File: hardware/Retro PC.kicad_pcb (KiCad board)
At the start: 2 copper layers, 160 x 160 mm, 70 parts, among them IC1 74HC00, IC10 W65C22, IC2 W65C02, IC3 74HC138, IC4 SYSTEM ROM, IC5 RAM, IC6 W65C22, IC7 W65C51, IC8 TL7702, IC9 FT232RL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

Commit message: Add BOM and Schematics
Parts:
- moved C14 70.8 mm to (283.8, 165.3)
- moved C18 70.8 mm to (262.6, 199.3)
- moved C2 70.8 mm to (225.8, 105.5)
- moved D12 70.8 mm to (292.8, 159.9)
- moved D3 70.8 mm to (271.7, 63.7)
- moved D9 70.8 mm to (274.3, 128.8)
- moved IC10 70.8 mm to (211.1, 199.3)
- moved IC2 70.8 mm to (243.6, 109.8)
- moved R7 70.8 mm to (289.0, 159.9)
- moved SW3 70.8 mm to (219.2, 63.3)
- moved X4 70.8 mm to (300.0, 189.7)
- moved C1 70.8 mm to (189.1, 144.2)
- moved C12 70.8 mm to (160.5, 81.3)
- moved C4 70.8 mm to (179.7, 120.6)
- moved C5 70.8 mm to (183.2, 146.5)
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
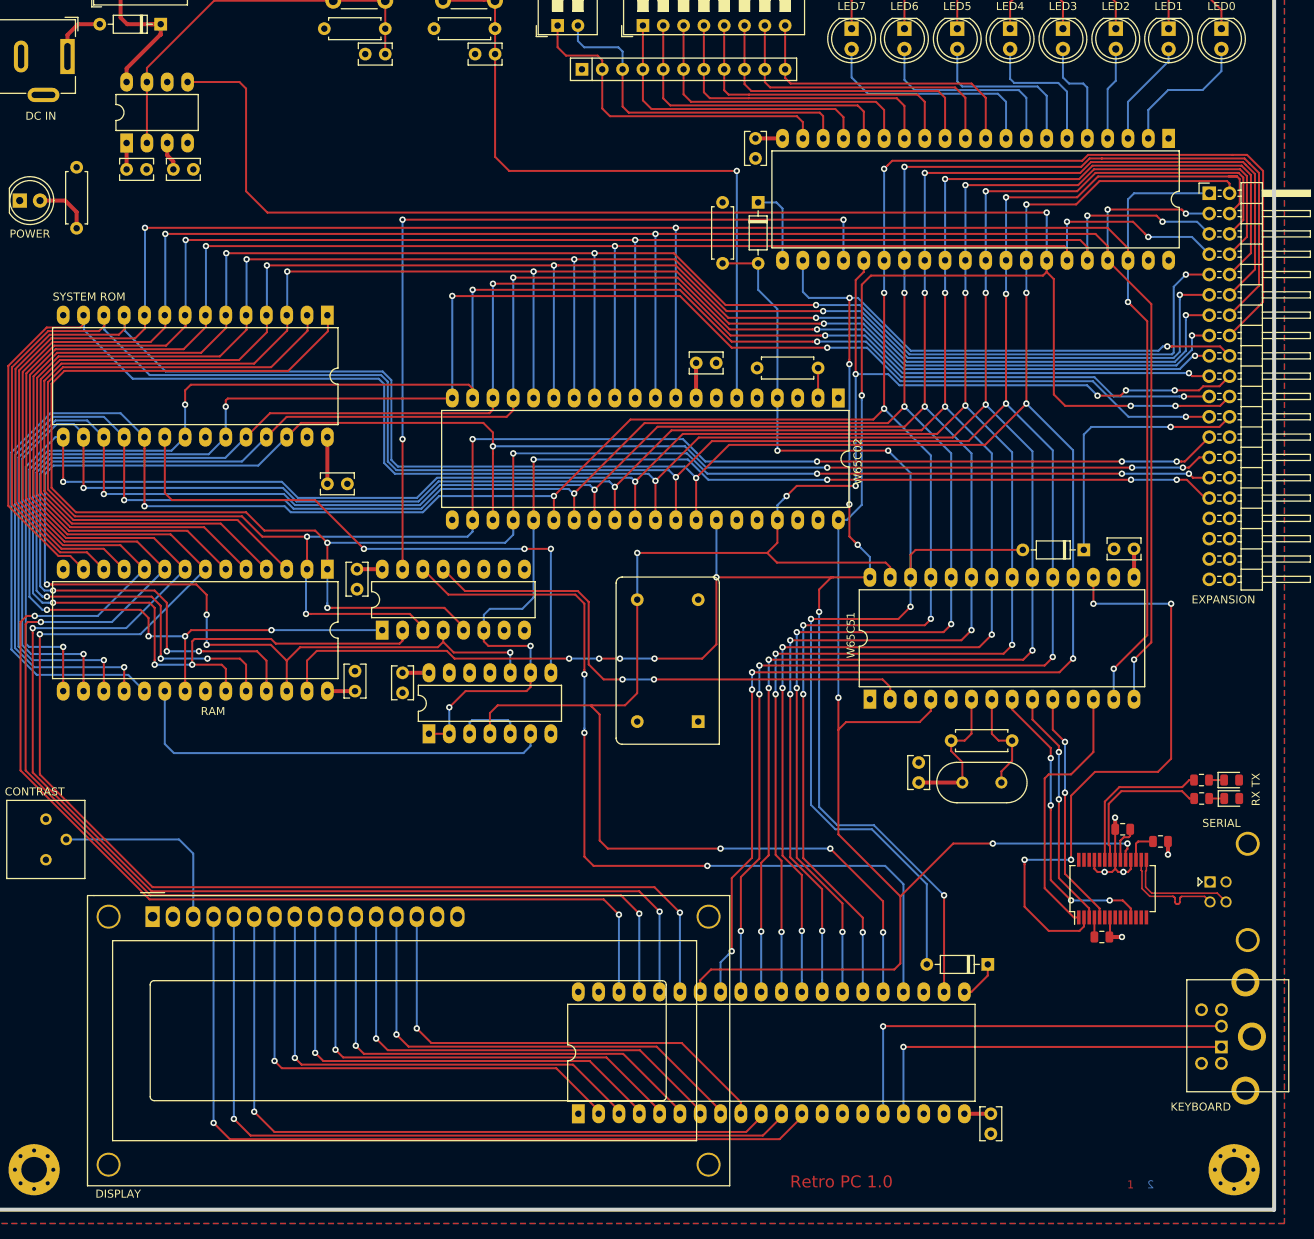
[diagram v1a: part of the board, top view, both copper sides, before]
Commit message: Finalize schematic and layout. Add switch for carrier detect
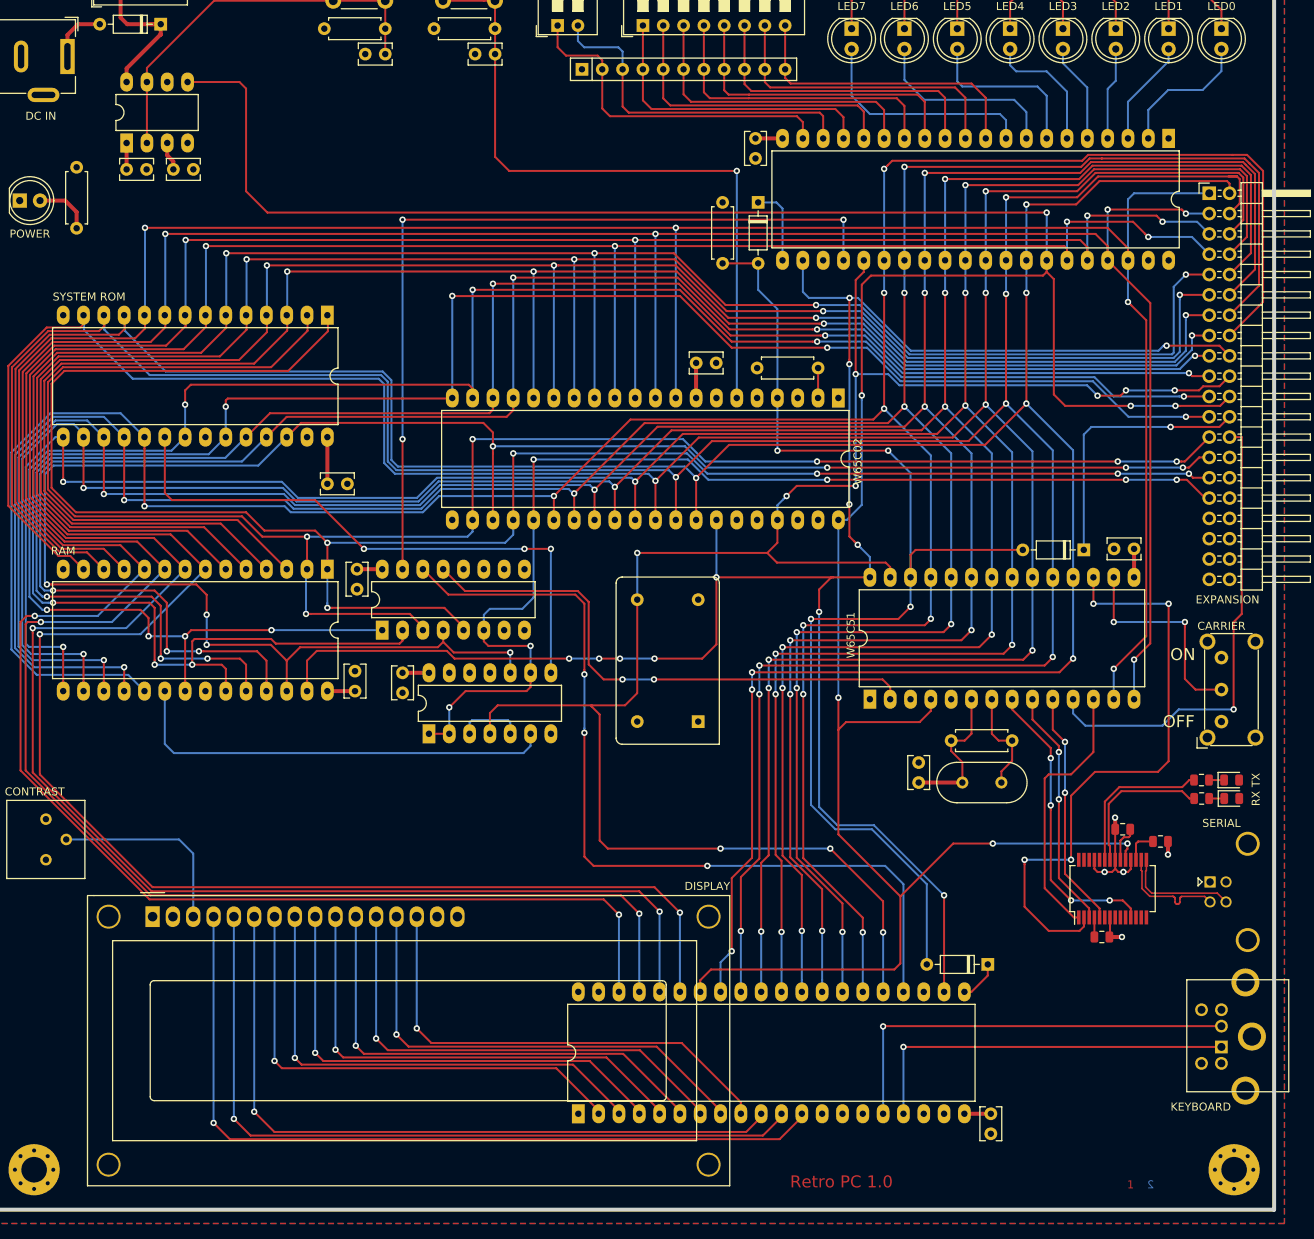
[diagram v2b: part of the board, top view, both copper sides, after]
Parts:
- added SW5: CARRIER, Button_Switch_THT:SW_E-Switch_EG1224_SPDT_Angled, F.Cu at (291.5, 150.3)
- IC8: value TL7702 -> TL7702A
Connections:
- net /Processor/RDY renamed Net-(IC2-Pad2)
- IC10 pad 13: (no net) -> Net-(IC10-Pad13)
- IC10 pad 14: (no net) -> Net-(IC10-Pad14)
- IC10 pad 15: (no net) -> Net-(IC10-Pad15)
- IC10 pad 18: (no net) -> Net-(IC10-Pad18)
- IC10 pad 19: (no net) -> Net-(IC10-Pad19)
- IC10 pad 39: (no net) -> Net-(IC10-Pad39)
- IC10 pad 40: (no net) -> Net-(IC10-Pad40)
- IC2 pad 1: (no net) -> Net-(IC2-Pad1)
- IC2 pad 3: (no net) -> Net-(IC2-Pad3)
- IC2 pad 35: (no net) -> Net-(IC2-Pad35)
- IC2 pad 36: (no net) -> Net-(IC2-Pad36)
- IC2 pad 38: (no net) -> Net-(IC2-Pad38)
- IC2 pad 39: (no net) -> Net-(IC2-Pad39)
- IC2 pad 5: (no net) -> Net-(IC2-Pad5)
- IC2 pad 7: (no net) -> Net-(IC2-Pad7)
- IC3 pad 10: (no net) -> Net-(IC3-Pad10)
- IC3 pad 11: (no net) -> Net-(IC3-Pad11)
- IC3 pad 12: (no net) -> Net-(IC3-Pad12)
- IC3 pad 7: (no net) -> Net-(IC3-Pad7)
- IC3 pad 9: (no net) -> Net-(IC3-Pad9)
- IC6 pad 39: (no net) -> Net-(IC6-Pad39)
- IC6 pad 40: (no net) -> Net-(IC6-Pad40)
- IC7 pad 11: (no net) -> /IO/~TerminalReady
- IC7 pad 16: (no net) -> /IO/~CarrierDetect
- IC7 pad 5: (no net) -> Net-(IC7-Pad5)
- IC8 pad 6: (no net) -> Net-(IC8-Pad6)
- IC9 pad 10: (no net) -> Net-(IC9-Pad10)
- IC9 pad 12: (no net) -> Net-(IC9-Pad12)
- IC9 pad 13: (no net) -> Net-(IC9-Pad13)
- IC9 pad 14: (no net) -> Net-(IC9-Pad14)
- IC9 pad 26: (no net) -> Net-(IC9-Pad26)
- IC9 pad 27: (no net) -> Net-(IC9-Pad27)
- IC9 pad 28: (no net) -> Net-(IC9-Pad28)
- IC9 pad 6: (no net) -> Net-(IC9-Pad6)
- IC9 pad 9: (no net) -> Net-(IC9-Pad9)
- RV1 pad 3: (no net) -> Net-(RV1-Pad3)
- X2 pad 1: (no net) -> Net-(X2-Pad1)
- X3 pad 26: (no net) -> /IO/~TerminalReady
- X3 pad 28: (no net) -> Net-(X3-Pad28)
- X3 pad 30: (no net) -> Net-(X3-Pad30)
- X3 pad 32: (no net) -> Net-(X3-Pad32)
- X3 pad 33: (no net) -> Net-(X3-Pad33)
- X3 pad 34: (no net) -> Net-(X3-Pad34)
- X3 pad 35: (no net) -> Net-(X3-Pad35)
- X3 pad 36: (no net) -> Net-(X3-Pad36)
- X3 pad 37: (no net) -> Net-(X3-Pad37)
- X3 pad 38: (no net) -> Net-(X3-Pad38)
- X4 pad 3: (no net) -> Net-(X4-Pad3)
- X4 pad 6: (no net) -> Net-(X4-Pad6)
- XTAL1 pad 1: (no net) -> Net-(XTAL1-Pad1)
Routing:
- net /IO/~TerminalReady: track 0.00 -> 59.3 mm, vias 0 -> 1
- net /IO/~CarrierDetect: track 0.00 -> 26.7 mm, vias 0 -> 2
- net /IO/PA6: track 25.1 -> 24.1 mm
- net /IO/PA3: track 13.5 -> 12.4 mm
- net /IO/PA4: track 17.3 -> 16.4 mm
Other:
- board text added: "OFF"
- board text added: "ON"
